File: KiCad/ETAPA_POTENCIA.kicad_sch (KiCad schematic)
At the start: 13 parts, among them U1 LM1117DT-3.3, U4 LM2596S-5

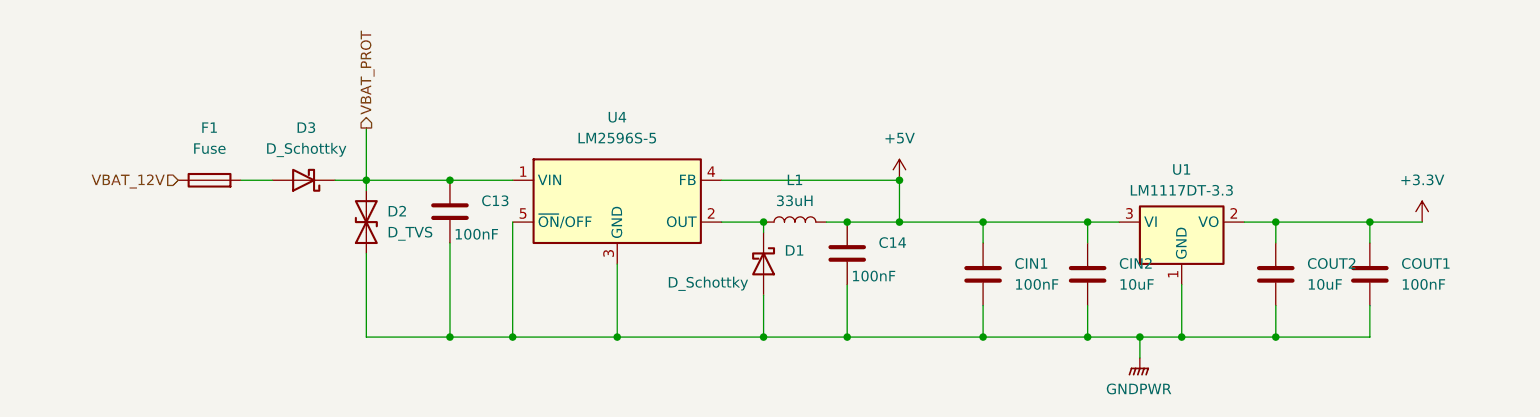
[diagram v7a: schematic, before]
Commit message: Correció etapa d'alimentació e Inputs
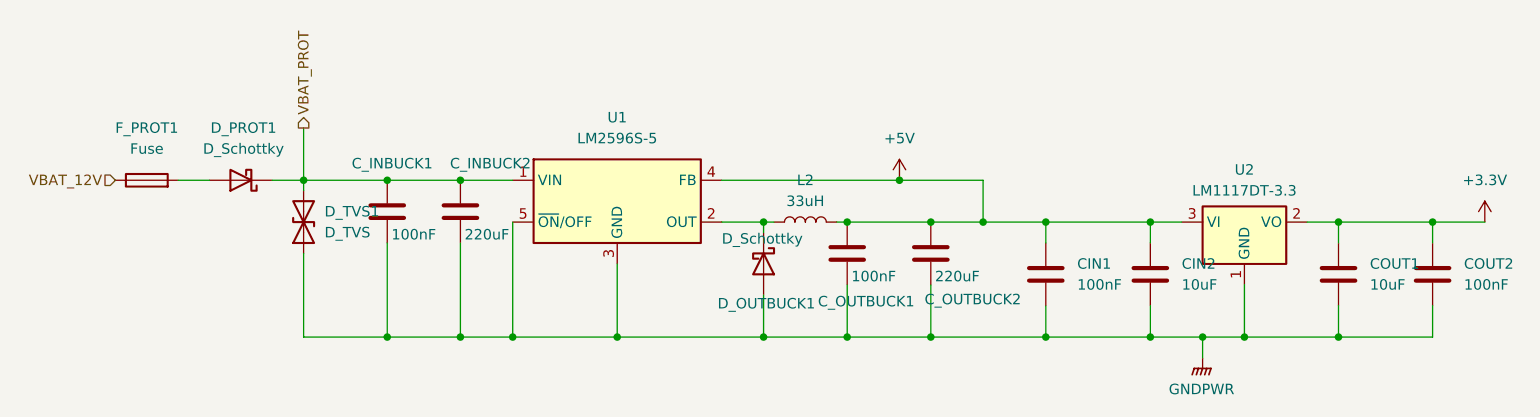
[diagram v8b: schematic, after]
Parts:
- removed L1: 33uH, symbol Device:L
- added C_INBUCK2, C_OUTBUCK2: 220uF, Capacitor_SMD:CP_Elec_8x10, symbol Device:C
- added L2: 33uH, Inductor_SMD:L_10.4x10.4_H4.8, symbol Device:L
- CIN1: footprint (none) -> Capacitor_SMD:C_0805_2012Metric
- CIN2: footprint (none) -> Capacitor_SMD:C_1206_3216Metric
- COUT1: renamed from COUT2; footprint (none) -> Capacitor_SMD:C_1206_3216Metric
- COUT2: renamed from COUT1; footprint (none) -> Capacitor_SMD:C_0805_2012Metric
- C_INBUCK1: renamed from C13; footprint (none) -> Capacitor_SMD:C_0805_2012Metric
- C_OUTBUCK1: renamed from C14; footprint (none) -> Capacitor_SMD:C_0805_2012Metric
- D_OUTBUCK1: renamed from D1; footprint (none) -> Diode_SMD:D_SMB_Modified
- D_PROT1: renamed from D3; footprint (none) -> Diode_SMD:D_SMB_Modified
- D_TVS1: renamed from D2; footprint (none) -> Diode_SMD:D_SMB_Modified
- F_PROT1: renamed from F1; footprint (none) -> Fuse:Fuse_1812_4532Metric
- renumbered U4 to U1, U1 to U2
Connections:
- net +5V: now also C_OUTBUCK2.1, L2.2
- net GNDPWR: now also C_INBUCK2.2, C_OUTBUCK2.2
- net VBAT_PROT: now also C_INBUCK2.1
- net at D_OUTBUCK1.1 (K), U1.2 (OUT): now also L2.1
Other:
- moved on the sheet: CIN1, CIN2, COUT1, COUT2, C_INBUCK1, D_PROT1, D_TVS1, F_PROT1, U2
